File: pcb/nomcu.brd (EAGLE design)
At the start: 69.4 x 69 mm, 38 parts, among them IC4 MY_7905DT, J1 ATX24RH

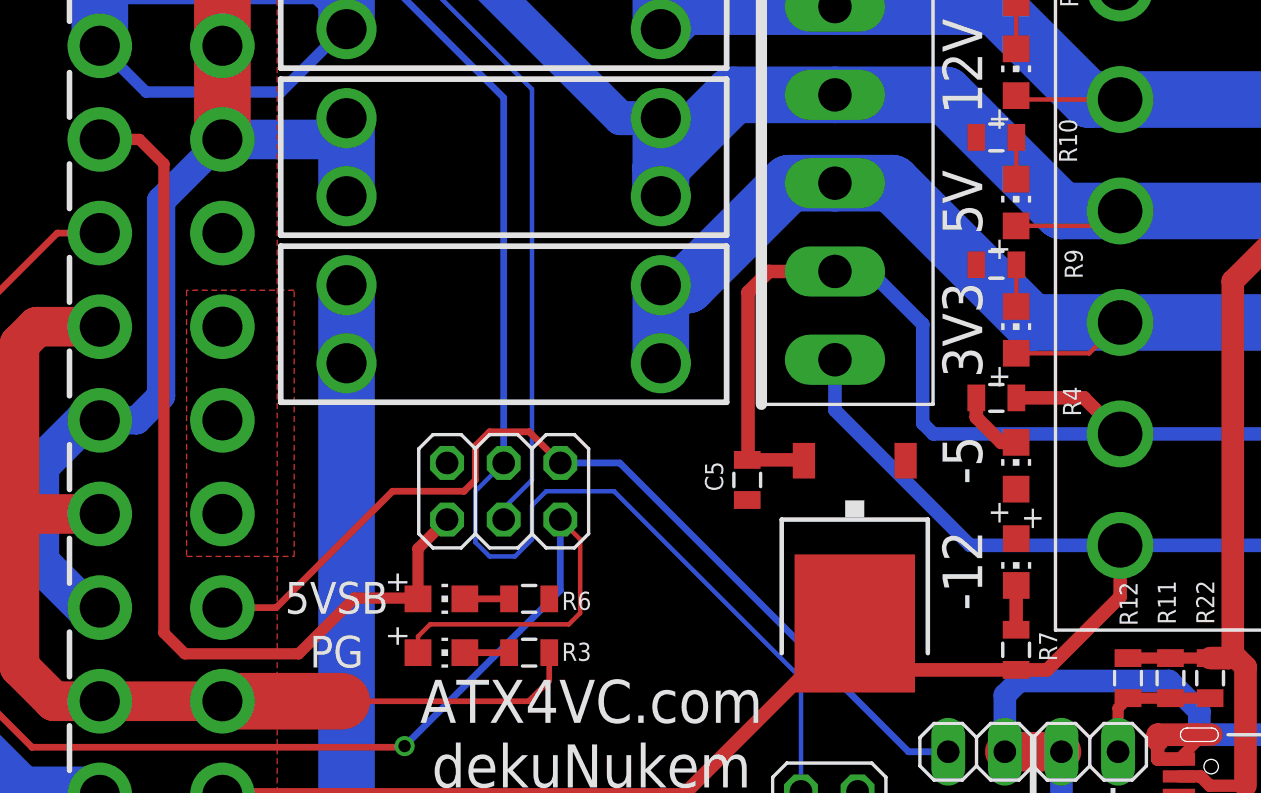
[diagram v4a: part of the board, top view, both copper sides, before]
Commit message: cleaned up traces
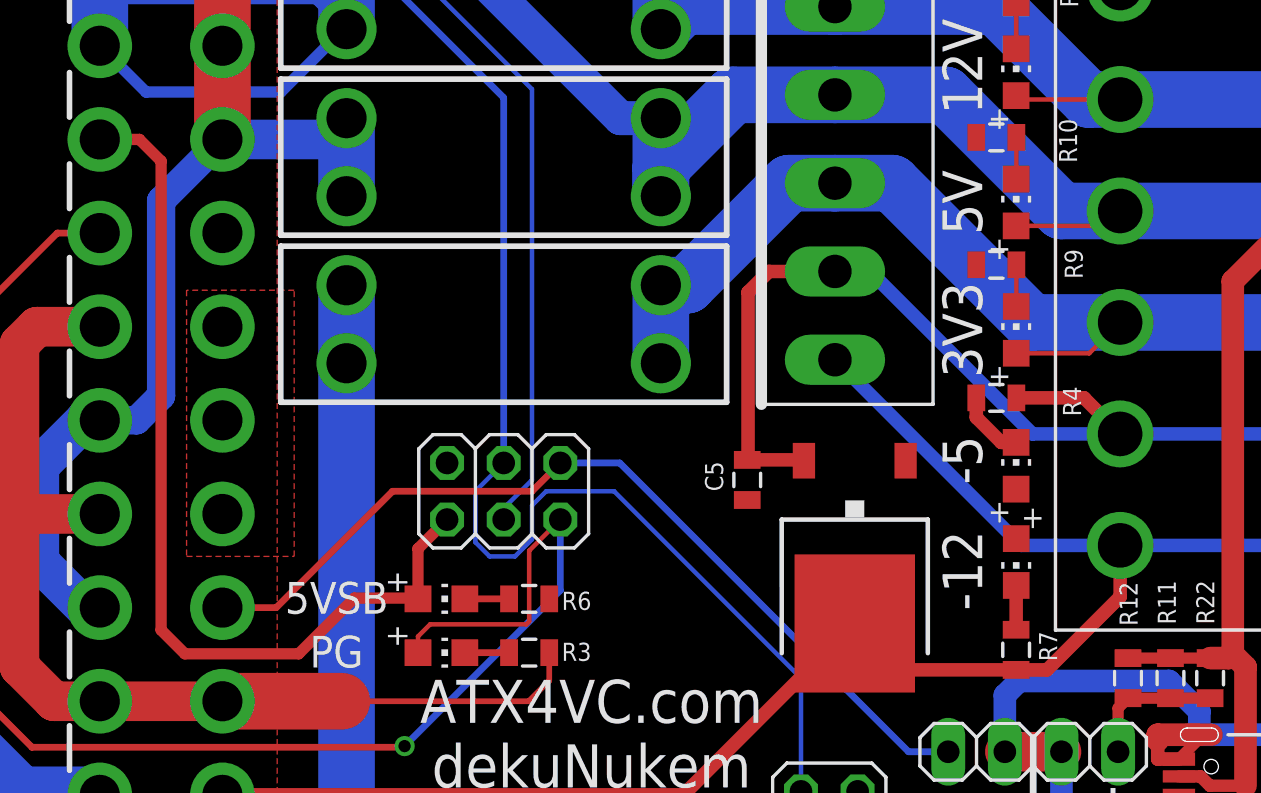
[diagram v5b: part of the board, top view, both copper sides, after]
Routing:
- net -5V: track 46.4 -> 43.8 mm
- net N$15: track 42.7 -> 40.6 mm
- net N$11: track 70.3 -> 68.4 mm
- net -12V: track 73.7 -> 72.4 mm
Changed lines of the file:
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@@
 <grid distance="5" unitdist="mil" unit="mil" style="lines" multiple="1" display="no" altdistance="1" altunitdist="mil" altunit="mil"/>
 <layers>
-<layer number="1" name="Top" color="4" fill="1" visible="yes" active="yes"/>
+<layer number="1" name="Top" color="4" fill="1" visible="no" active="yes"/>
 <layer number="2" name="Route2" color="16" fill="1" visible="no" active="no"/>
 <layer number="3" name="Route3" color="17" fill="1" visible="no" active="no"/>
@@
 <layer number="19" name="Unrouted" color="6" fill="1" visible="yes" active="yes"/>
 <layer number="20" name="Dimension" color="24" fill="1" visible="yes" active="yes"/>
-<layer number="21" name="tPlace" color="7" fill="1" visible="yes" active="yes"/>
-<layer number="22" name="bPlace" color="7" fill="1" visible="yes" active="yes"/>
-<layer number="23" name="tOrigins" color="15" fill="1" visible="yes" active="yes"/>
+<layer number="21" name="tPlace" color="7" fill="1" visible="no" active="yes"/>
+<layer number="22" name="bPlace" color="7" fill="1" visible="no" active="yes"/>
+<layer number="23" name="tOrigins" color="15" fill="1" visible="no" active="yes"/>
 <layer number="24" name="bOrigins" color="15" fill="1" visible="yes" active="yes"/>
-<layer number="25" name="tNames" color="7" fill="1" visible="yes" active="yes"/>
-<layer number="26" name="bNames" color="7" fill="1" visible="yes" active="yes"/>
-<layer number="27" name="tValues" color="7" fill="1" visible="yes" active="yes"/>
-<layer number="28" name="bValues" color="7" fill="1" visible="yes" active="yes"/>
+<layer number="25" name="tNames" color="7" fill="1" visible="no" active="yes"/>
+<layer number="26" name="bNames" color="7" fill="1" visible="no" active="yes"/>
+<layer number="27" name="tValues" color="7" fill="1" visible="no" active="yes"/>
+<layer number="28" name="bValues" color="7" fill="1" visible="no" active="yes"/>
 <layer number="29" name="tStop" color="7" fill="3" visible="no" active="yes"/>
 <layer number="30" name="bStop" color="7" fill="6" visible="no" active="yes"/>
@@
 <layer number="37" name="tTest" color="7" fill="1" visible="no" active="yes"/>
 <layer number="38" name="bTest" color="7" fill="1" visible="no" active="yes"/>
-<layer number="39" name="tKeepout" color="4" fill="11" visible="yes" active="yes"/>
+<layer number="39" name="tKeepout" color="4" fill="11" visible="no" active="yes"/>
 <layer number="40" name="bKeepout" color="1" fill="11" visible="yes" active="yes"/>
-<layer number="41" name="tRestrict" color="4" fill="10" visible="yes" active="yes"/>
+<layer number="41" name="tRestrict" color="4" fill="10" visible="no" active="yes"/>
 <layer number="42" name="bRestrict" color="1" fill="10" visible="yes" active="yes"/>
 <layer number="43" name="vRestrict" color="2" fill="10" visible="no" active="yes"/>
 <layer number="44" name="Drills" color="7" fill="1" visible="no" active="yes"/>
-<layer number="45" name="Holes" color="7" fill="1" visible="yes" active="yes"/>
+<layer number="45" name="Holes" color="7" fill="1" visible="no" active="yes"/>
 <layer number="46" name="Milling" color="3" fill="1" visible="yes" active="yes"/>
 <layer number="47" name="Measures" color="7" fill="1" visible="no" active="yes"/>
@@
 <layer number="49" name="Reference" color="7" fill="1" visible="no" active="yes"/>
 <layer number="50" name="dxf" color="7" fill="1" visible="no" active="no"/>
-<layer number="51" name="tDocu" color="7" fill="1" visible="yes" active="yes"/>
-<layer number="52" name="bDocu" color="7" fill="1" visible="yes" active="yes"/>
+<layer number="51" name="tDocu" color="7" fill="1" visible="no" active="yes"/>
+<layer number="52" name="bDocu" color="7" fill="1" visible="no" active="yes"/>
 <layer number="53" name="tGND_GNDA" color="7" fill="1" visible="no" active="no"/>
 <layer number="54" name="bGND_GNDA" color="7" fill="1" visible="no" active="no"/>
@@
 <contactref element="J1" pad="9"/>
 <contactref element="LED2" pad="A"/>
-<wire x1="16.256" y1="44.401" x2="15.157" y2="45.5" width="0.508" layer="1"/>
+<wire x1="16.129" y1="44.528" x2="15.157" y2="45.5" width="0.508" layer="1"/>
 <wire x1="13.379" y1="45.5" x2="15.157" y2="45.5" width="0.508" layer="1"/>
 <wire x1="27.686" y1="24.926" x2="27.652" y2="24.892" width="0.508" layer="1"/>
 <wire x1="24.799" y1="24.926" x2="27.686" y2="24.926" width="0.508" layer="1"/>
-<wire x1="16.256" y1="44.401" x2="16.256" y2="23.368" width="0.508" layer="1"/>
-<wire x1="16.256" y1="23.368" x2="17.1958" y2="22.4282" width="0.508" layer="1"/>
+<wire x1="16.129" y1="44.528" x2="16.129" y2="23.495" width="0.508" layer="1"/>
+<wire x1="16.129" y1="23.495" x2="17.1958" y2="22.4282" width="0.508" layer="1"/>
 <wire x1="17.1958" y1="22.4282" x2="22.3012" y2="22.4282" width="0.508" layer="1"/>
 <wire x1="22.3012" y1="22.4282" x2="24.799" y2="24.926" width="0.508" layer="1"/>
@@
 <contactref element="U$9" pad="P$13"/>
 <contactref element="U$9" pad="P$14"/>
-<wire x1="52.415" y1="27.291" x2="46.355" y2="33.351" width="0.6096" layer="16"/>
-<wire x1="46.355" y1="35.618" x2="46.355" y2="33.351" width="0.6096" layer="16"/>
-<wire x1="52.415" y1="27.291" x2="59.146" y2="27.291" width="0.6096" layer="16"/>
+<wire x1="54.701" y1="27.291" x2="46.374" y2="35.618" width="0.6096" layer="16"/>
+<wire x1="46.355" y1="35.618" x2="46.374" y2="35.618" width="0.6096" layer="16"/>
+<wire x1="54.701" y1="27.291" x2="59.146" y2="27.291" width="0.6096" layer="16"/>
 <wire x1="59.146" y1="27.291" x2="67.346" y2="27.291" width="0.6096" layer="16"/>
 <wire x1="59.146" y1="27.291" x2="59.146" y2="24.983" width="0.6096" layer="1"/>
@@
 <wire x1="57.53" y1="33.907" x2="59.146" y2="32.291" width="0.6096" layer="1"/>
 <wire x1="46.355" y1="39.578" x2="47.925" y2="39.578" width="0.6096" layer="16"/>
-<wire x1="50.292" y1="37.211" x2="50.292" y2="32.766" width="0.6096" layer="16"/>
-<wire x1="47.925" y1="39.578" x2="50.292" y2="37.211" width="0.6096" layer="16"/>
-<wire x1="50.292" y1="32.766" x2="50.767" y2="32.291" width="0.6096" layer="16"/>
-<wire x1="50.767" y1="32.291" x2="59.146" y2="32.291" width="0.6096" layer="16"/>
+<wire x1="47.925" y1="39.578" x2="55.212" y2="32.291" width="0.6096" layer="16"/>
+<wire x1="55.212" y1="32.291" x2="59.146" y2="32.291" width="0.6096" layer="16"/>
 <wire x1="42.457" y1="31.089" x2="42.42" y2="31.126" width="0.6096" layer="1"/>
 <wire x1="46.355" y1="39.578" x2="43.388" y2="39.578" width="0.6096" layer="1"/>
@@
 <wire x1="7.874" y1="20.701" x2="10.3378" y2="18.2372" width="0.3048" layer="1"/>
 <wire x1="27.652" y1="22.479" x2="27.652" y2="23.207" width="0.2032" layer="1"/>
-<wire x1="34.417" y1="23.749" x2="34.925" y2="24.257" width="0.2032" layer="1"/>
-<wire x1="34.925" y1="24.257" x2="34.925" y2="27.559" width="0.2032" layer="1"/>
-<wire x1="34.925" y1="27.559" x2="34.036" y2="28.448" width="0.2032" layer="1"/>
 <wire x1="27.652" y1="23.207" x2="28.194" y2="23.749" width="0.2032" layer="1"/>
-<wire x1="28.194" y1="23.749" x2="34.417" y2="23.749" width="0.2032" layer="1"/>
 <via x="27.051" y="18.288" extent="1-16" drill="0.55"/>
 <wire x1="27.051" y1="18.288" x2="34.036" y2="25.273" width="0.3048" layer="16"/>
@@
 <wire x1="27.0002" y1="18.2372" x2="27.051" y2="18.288" width="0.3048" layer="1"/>
 <wire x1="27.0002" y1="18.2372" x2="10.3378" y2="18.2372" width="0.3048" layer="1"/>
+<wire x1="28.194" y1="23.749" x2="32.512" y2="23.749" width="0.2032" layer="1"/>
+<wire x1="32.639" y1="27.051" x2="34.036" y2="28.448" width="0.2032" layer="1"/>
+<wire x1="32.512" y1="23.749" x2="32.639" y2="23.876" width="0.2032" layer="1"/>
+<wire x1="32.639" y1="23.876" x2="32.639" y2="27.051" width="0.2032" layer="1"/>
 </signal>
 <signal name="N$15">
@@
 <contactref element="JP3" pad="6"/>
 <wire x1="36.703" y1="30.988" x2="34.036" y2="30.988" width="0.3048" layer="16"/>
-<wire x1="26.51" y1="29.718" x2="29.718" y2="29.718" width="0.3048" layer="1"/>
-<wire x1="30.226" y1="30.226" x2="30.226" y2="31.75" width="0.3048" layer="1"/>
-<wire x1="30.226" y1="31.75" x2="30.861" y2="32.385" width="0.3048" layer="1"/>
-<wire x1="32.639" y1="32.385" x2="34.036" y2="30.988" width="0.3048" layer="1"/>
-<wire x1="29.718" y1="29.718" x2="30.226" y2="30.226" width="0.3048" layer="1"/>
-<wire x1="30.861" y1="32.385" x2="32.639" y2="32.385" width="0.3048" layer="1"/>
+<wire x1="32.766" y1="29.718" x2="34.036" y2="30.988" width="0.3048" layer="1"/>
+<wire x1="26.51" y1="29.718" x2="32.766" y2="29.718" width="0.3048" layer="1"/>
 </signal>
 <signal name="N$3">
